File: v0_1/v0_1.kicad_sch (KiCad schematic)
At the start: 4 parts, among them J1 Z-ICS0S40P-W000, U1 Pico, U2 PCF8523T, U3 AHT20

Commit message: add charger ic
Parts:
- added IC1: TP4056-42-ESOP8, TP4056:SOIC127P600X175-9N, symbol TP4056-42-ESOP8:TP4056-42-ESOP8
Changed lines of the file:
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@@
     (pin "6")
     (instances
-      (project "Picowhttpsensor"
+      (project "v0_1"
         (path "/0bf090f4-b9b7-437f-9e6a-e818f47752ec"
           (reference "U3") (unit 1)
@@
     (pin "9")
     (instances
-      (project "Picowhttpsensor"
+      (project "v0_1"
         (path "/0bf090f4-b9b7-437f-9e6a-e818f47752ec"
           (reference "J1") (unit 1)
@@
     )
   )
+  (symbol (lib_id "TP4056-42-ESOP8:TP4056-42-ESOP8") (at 172.72 92.71 0) (unit 1)
+    (in_bom yes) (on_board yes) (dnp no) (fields_autoplaced)
+    (property "Reference" "IC1" (at 187.96 85.09 0)
+      (effects (font (size 1.27 1.27)))
+    )
+    (property "Value" "TP4056-42-ESOP8" (at 187.96 87.63 0)
+      (effects (font (size 1.27 1.27)))
+    )
+    (property "Footprint" "TP4056:SOIC127P600X175-9N" (at 199.39 90.17 0)
+      (effects (font (size 1.27 1.27)) (justify left) hide)
+    )
+    (property "Datasheet" "https://datasheet.lcsc.com/szlcsc/1906261508_Nanjing-Extension-Microelectronics-TP4056-42-ESOP8_C16581.pdf" (at 199.39 92.71 0)
+      (effects (font (size 1.27 1.27)) (justify left) hide)
+    )
+    (property "Description" "PMIC - Battery Management ESOP-8 RoHS" (at 199.39 95.25 0)
+      (effects (font (size 1.27 1.27)) (justify left) hide)
+    )
+    (property "Height" "1.75" (at 199.39 97.79 0)
+      (effects (font (size 1.27 1.27)) (justify left) hide)
+    )
+    (property "Manufacturer_Name" "Nanjing Extension Microelectronics" (at 199.39 100.33 0)
+      (effects (font (size 1.27 1.27)) (justify left) hide)
+    )
+    (property "Manufacturer_Part_Number" "TP4056-42-ESOP8" (at 199.39 102.87 0)
+      (effects (font (size 1.27 1.27)) (justify left) hide)
+    )
+    (property "Mouser Part Number" "" (at 199.39 105.41 0)
+      (effects (font (size 1.27 1.27)) (justify left) hide)
+    )
+    (property "Mouser Price/Stock" "" (at 199.39 107.95 0)
+      (effects (font (size 1.27 1.27)) (justify left) hide)
+    )
+    (property "Arrow Part Number" "" (at 199.39 110.49 0)
+      (effects (font (size 1.27 1.27)) (justify left) hide)
+    )
+    (property "Arrow Price/Stock" "" (at 199.39 113.03 0)
+      (effects (font (size 1.27 1.27)) (justify left) hide)
+    )
+    (pin "1")
+    (pin "2")
+    (pin "3")
+    (pin "4")
+    (pin "5")
+    (pin "6")
+    (pin "7")
+    (pin "8")
+    (pin "9")
+    (instances
+      (project "v0_1"
+        (path "/0bf090f4-b9b7-437f-9e6a-e818f47752ec"
+          (reference "IC1") (unit 1)
+        )
+      )
+    )
+  )
   (symbol (lib_id "MCU_RaspberryPi_and_Boards:Pico") (at 133.35 88.9 0) (unit 1)
-    (in_bom yes) (on_board yes) (dnp no) (fields_autoplaced)
+    (in_bom yes) (on_board yes) (dnp no)
     (property "Reference" "U1" (at 133.35 57.15 0)
       (effects (font (size 1.27 1.27)))
@@
     (pin "9")
     (instances
-      (project "Picowhttpsensor"
+      (project "v0_1"
         (path "/0bf090f4-b9b7-437f-9e6a-e818f47752ec"
           (reference "U1") (unit 1)
@@
     (pin "8")
     (instances
-      (project "Picowhttpsensor"
+      (project "v0_1"
         (path "/0bf090f4-b9b7-437f-9e6a-e818f47752ec"
           (reference "U2") (unit 1)

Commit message: add aht20
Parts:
- removed IC1: TP4056-42-ESOP8, TP4056:SOIC127P600X175-9N, symbol TP4056-42-ESOP8:TP4056-42-ESOP8
- removed U2: PCF8523T, Package_SO:SOIC-8_3.9x4.9mm_P1.27mm, symbol Timer_RTC:PCF8523T
- removed U3: AHT20, AHT20:AHT20, symbol AHT20:AHT20
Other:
- added sheet AHT20 (TemperatureSensor.kicad_sch)
- added sheet PCF8523T (RTC.kicad_sch)
- added sheet TP4056 (ChargerIC.kicad_sch)
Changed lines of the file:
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@@
     (title "Picohttpsensor")
-  )
-  (symbol (lib_id "AHT20:AHT20") (at 220.98 100.33 0) (unit 1)
-    (in_bom yes) (on_board yes) (dnp no) (fields_autoplaced)
-    (property "Reference" "U3" (at 234.95 92.71 0)
-      (effects (font (size 1.27 1.27)))
-    )
-    (property "Value" "AHT20" (at 234.95 95.25 0)
-      (effects (font (size 1.27 1.27)))
-    )
-    (property "Footprint" "AHT20:AHT20" (at 245.11 97.79 0)
-      (effects (font (size 1.27 1.27)) (justify left) hide)
-    )
-    (property "Datasheet" "http://www.aosong.com/userfiles/files/media/Data%20Sheet%20AHT20.pdf" (at 245.11 100.33 0)
-      (effects (font (size 1.27 1.27)) (justify left) hide)
-    )
-    (property "Description" "Integrated temperature and humidity Sensor DC : 2.2 - 5.5V, 0 ~{} 100% RH, -40 ~{} + 85 ." (at 245.11 102.87 0)
-      (effects (font (size 1.27 1.27)) (justify left) hide)
-    )
-    (property "Height" "1.1" (at 245.11 105.41 0)
-      (effects (font (size 1.27 1.27)) (justify left) hide)
-    )
-    (property "Manufacturer_Name" "Aosong" (at 245.11 107.95 0)
-      (effects (font (size 1.27 1.27)) (justify left) hide)
-    )
-    (property "Manufacturer_Part_Number" "AHT20" (at 245.11 110.49 0)
-      (effects (font (size 1.27 1.27)) (justify left) hide)
-    )
-    (property "Mouser Part Number" "" (at 245.11 113.03 0)
-      (effects (font (size 1.27 1.27)) (justify left) hide)
-    )
-    (property "Mouser Price/Stock" "" (at 245.11 115.57 0)
-      (effects (font (size 1.27 1.27)) (justify left) hide)
-    )
-    (property "Arrow Part Number" "" (at 245.11 118.11 0)
-      (effects (font (size 1.27 1.27)) (justify left) hide)
-    )
-    (property "Arrow Price/Stock" "" (at 245.11 120.65 0)
-      (effects (font (size 1.27 1.27)) (justify left) hide)
-    )
-    (pin "1")
-    (pin "2")
-    (pin "3")
-    (pin "4")
-    (pin "5")
-    (pin "6")
-    (instances
-      (project "v0_1"
-        (path "/0bf090f4-b9b7-437f-9e6a-e818f47752ec"
-          (reference "U3") (unit 1)
-        )
-      )
-    )
   )
   (symbol (lib_id "Z-ICS0S40P-W000:Z-ICS0S40P-W000") (at 69.85 66.04 0) (unit 1)
@@
     )
   )
-  (symbol (lib_id "TP4056-42-ESOP8:TP4056-42-ESOP8") (at 172.72 92.71 0) (unit 1)
-    (in_bom yes) (on_board yes) (dnp no) (fields_autoplaced)
-    (property "Reference" "IC1" (at 187.96 85.09 0)
-      (effects (font (size 1.27 1.27)))
-    )
-    (property "Value" "TP4056-42-ESOP8" (at 187.96 87.63 0)
-      (effects (font (size 1.27 1.27)))
-    )
-    (property "Footprint" "TP4056:SOIC127P600X175-9N" (at 199.39 90.17 0)
-      (effects (font (size 1.27 1.27)) (justify left) hide)
-    )
-    (property "Datasheet" "https://datasheet.lcsc.com/szlcsc/1906261508_Nanjing-Extension-Microelectronics-TP4056-42-ESOP8_C16581.pdf" (at 199.39 92.71 0)
-      (effects (font (size 1.27 1.27)) (justify left) hide)
-    )
-    (property "Description" "PMIC - Battery Management ESOP-8 RoHS" (at 199.39 95.25 0)
-      (effects (font (size 1.27 1.27)) (justify left) hide)
-    )
-    (property "Height" "1.75" (at 199.39 97.79 0)
-      (effects (font (size 1.27 1.27)) (justify left) hide)
-    )
-    (property "Manufacturer_Name" "Nanjing Extension Microelectronics" (at 199.39 100.33 0)
-      (effects (font (size 1.27 1.27)) (justify left) hide)
-    )
-    (property "Manufacturer_Part_Number" "TP4056-42-ESOP8" (at 199.39 102.87 0)
-      (effects (font (size 1.27 1.27)) (justify left) hide)
-    )
-    (property "Mouser Part Number" "" (at 199.39 105.41 0)
-      (effects (font (size 1.27 1.27)) (justify left) hide)
-    )
-    (property "Mouser Price/Stock" "" (at 199.39 107.95 0)
-      (effects (font (size 1.27 1.27)) (justify left) hide)
-    )
-    (property "Arrow Part Number" "" (at 199.39 110.49 0)
-      (effects (font (size 1.27 1.27)) (justify left) hide)
-    )
-    (property "Arrow Price/Stock" "" (at 199.39 113.03 0)
-      (effects (font (size 1.27 1.27)) (justify left) hide)
-    )
-    (pin "1")
-    (pin "2")
-    (pin "3")
-    (pin "4")
-    (pin "5")
-    (pin "6")
-    (pin "7")
-    (pin "8")
-    (pin "9")
-    (instances
-      (project "v0_1"
-        (path "/0bf090f4-b9b7-437f-9e6a-e818f47752ec"
-          (reference "IC1") (unit 1)
-        )
-      )
-    )
-  )
   (symbol (lib_id "MCU_RaspberryPi_and_Boards:Pico") (at 133.35 88.9 0) (unit 1)
     (in_bom yes) (on_board yes) (dnp no)
@@
     )
   )
-  (symbol (lib_id "Timer_RTC:PCF8523T") (at 226.06 76.2 0) (unit 1)
-    (in_bom yes) (on_board yes) (dnp no) (fields_autoplaced)
-    (property "Reference" "U2" (at 242.57 72.5521 0)
-      (effects (font (size 1.27 1.27)))
+  (sheet (at 180.34 91.44) (size 31.75 6.35) (fields_autoplaced)
+    (stroke (width 0.1524) (type solid))
+    (fill (color 0 0 0 0.0000))
+    (property "Sheetname" "AHT20" (at 180.34 90.7284 0)
+      (effects (font (size 1.27 1.27)) (justify left bottom))
     )
-    (property "Value" "PCF8523T" (at 242.57 75.0921 0)
-      (effects (font (size 1.27 1.27)))
+    (property "Sheetfile" "TemperatureSensor.kicad_sch" (at 180.34 98.3746 0)
+      (effects (font (size 1.27 1.27)) (justify left top))
     )
-    (property "Footprint" "Package_SO:SOIC-8_3.9x4.9mm_P1.27mm" (at 246.38 85.09 0)
-      (effects (font (size 1.27 1.27)) hide)
-    )
-    (property "Datasheet" "https://www.nxp.com/docs/en/data-sheet/PCF8523.pdf" (at 226.06 76.2 0)
-      (effects (font (size 1.27 1.27)) hide)
-    )
-    (pin "1")
-    (pin "2")
-    (pin "3")
-    (pin "4")
-    (pin "5")
-    (pin "6")
-    (pin "7")
-    (pin "8")
     (instances
       (project "v0_1"
-        (path "/0bf090f4-b9b7-437f-9e6a-e818f47752ec"
-          (reference "U2") (unit 1)
-        )
+        (path "/0bf090f4-b9b7-437f-9e6a-e818f47752ec" (page "4"))
       )
     )
+  )
+  (sheet (at 180.34 66.04) (size 31.75 6.35) (fields_autoplaced)
+    (stroke (width 0.1524) (type solid))
+    (fill (color 0 0 0 0.0000))
+    (property "Sheetname" "TP4056" (at 180.34 65.3284 0)
+      (effects (font (size 1.27 1.27)) (justify left bottom))
+    )
+    (property "Sheetfile" "ChargerIC.kicad_sch" (at 180.34 72.9746 0)
+      (effects (font (size 1.27 1.27)) (justify left top))
+    )
+    (instances
+      (project "v0_1"
+        (path "/0bf090f4-b9b7-437f-9e6a-e818f47752ec" (page "2"))
+      )
+    )
+  )
+  (sheet (at 180.34 78.74) (size 31.75 6.35) (fields_autoplaced)
+    (stroke (width 0.1524) (type solid))
+    (fill (color 0 0 0 0.0000))
+    (property "Sheetname" "PCF8523T" (at 180.34 78.0284 0)
+      (effects (font (size 1.27 1.27)) (justify left bottom))
+    )
+    (property "Sheetfile" "RTC.kicad_sch" (at 180.34 85.6746 0)
+      (effects (font (size 1.27 1.27)) (justify left top))
+    )
+    (instances
+      (project "v0_1"
+        (path "/0bf090f4-b9b7-437f-9e6a-e818f47752ec" (page "3"))
+      )
+    )

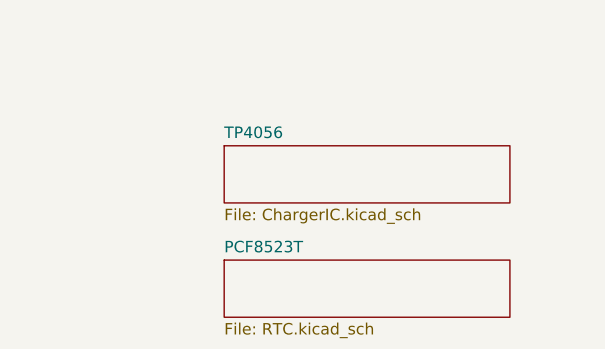
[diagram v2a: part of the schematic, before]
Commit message: add rtc and charger schematic
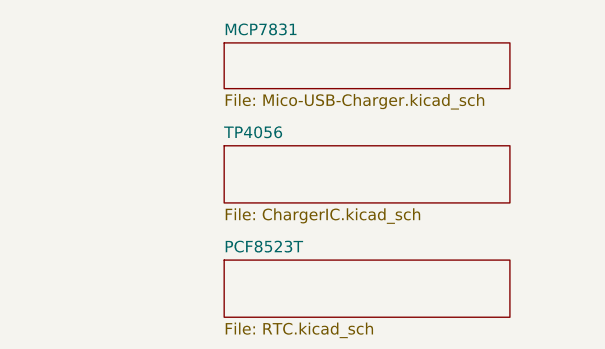
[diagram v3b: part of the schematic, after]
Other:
- added sheet MCP7831 (Mico-USB-Charger.kicad_sch)
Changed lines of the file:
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@@
+    )
+  )
+  (sheet (at 180.34 54.61) (size 31.75 5.08) (fields_autoplaced)
+    (stroke (width 0.1524) (type solid))
+    (fill (color 0 0 0 0.0000))
+    (property "Sheetname" "MCP7831" (at 180.34 53.8984 0)
+      (effects (font (size 1.27 1.27)) (justify left bottom))
+    )
+    (property "Sheetfile" "Mico-USB-Charger.kicad_sch" (at 180.34 60.2746 0)
+      (effects (font (size 1.27 1.27)) (justify left top))
+    )
+    (instances
+      (project "v0_1"
+        (path "/0bf090f4-b9b7-437f-9e6a-e818f47752ec" (page "5"))
+      )
     )
   )

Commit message: add 0.2V
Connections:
- net PCF8523T/MISO: now reaches U1.21 (GPIO16)
- net PCF8523T/SD_CS: now reaches U1.22 (GPIO17)
- net GND: now reaches U1.23 (GND)
- net GND: now also U1.28 (GND), U1.3 (GND), U1.38 (GND), U1.8 (GND)
- net PCF8523T/SCK: now reaches U1.24 (GPIO18)
- net PCF8523T/MOSI: now reaches U1.25 (GPIO19)
- net +3.3V: now reaches U1.36 (3V3)
- net SCL: now reaches U1.6 (GPIO4)
- net SDA: now reaches U1.7 (GPIO5)
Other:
- sheet AHT20 ports: added SCL, SDA; removed none
- sheet PCF8523T ports: added MISO, MOSI, SCK, SCL, SDA, SD_CS; removed none
- moved on the sheet: J1, U1
